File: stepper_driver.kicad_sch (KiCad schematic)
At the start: 8 parts, among them J1 Conn_01x04_Pin, U3 TMC2208_SILENTSTEPSTICK

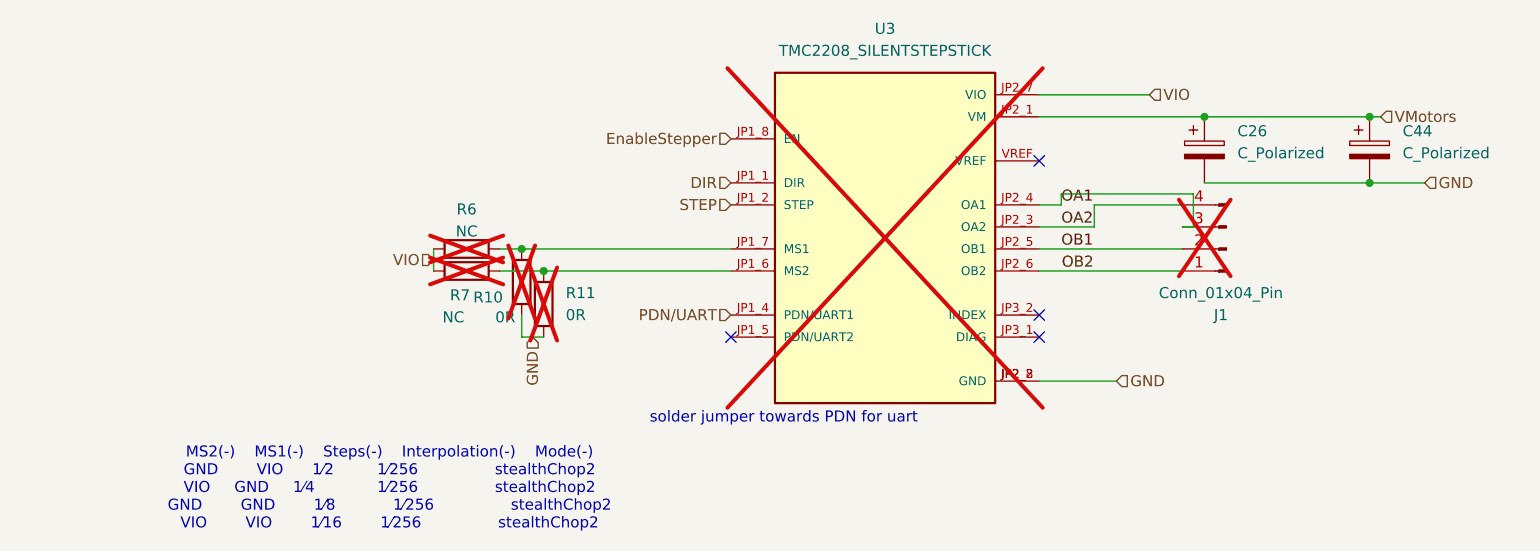
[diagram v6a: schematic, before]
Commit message: fix DNP (was just for checking what was to be bought)
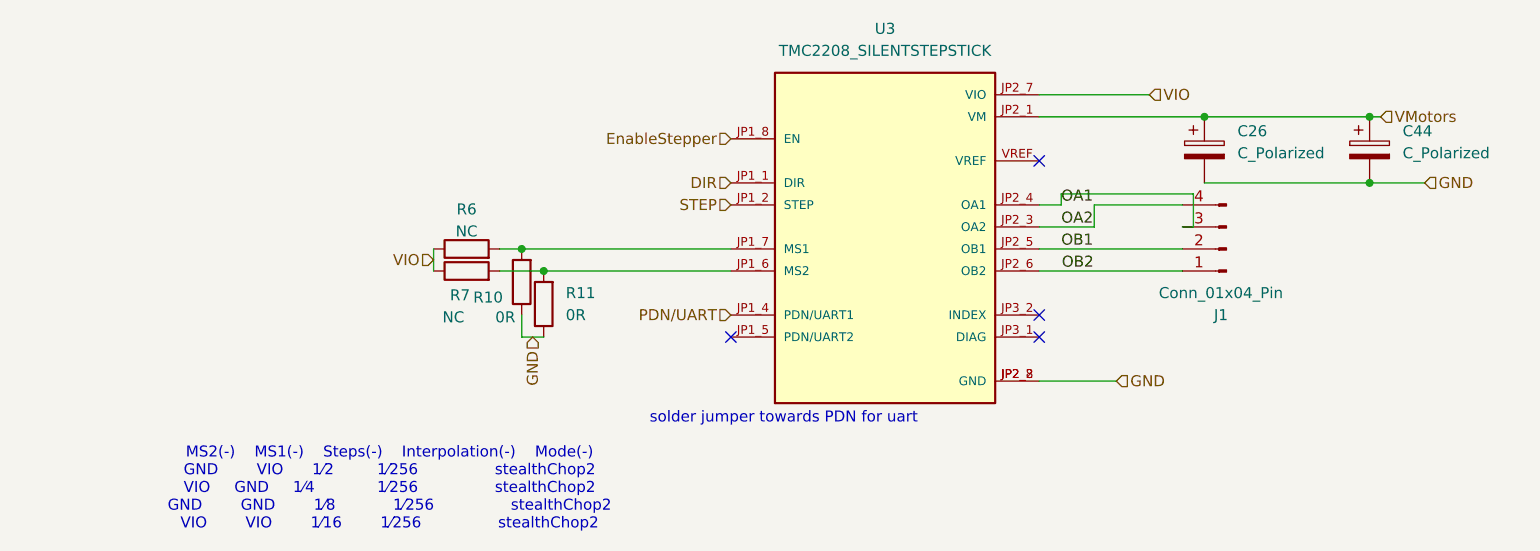
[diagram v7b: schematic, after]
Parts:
- J1, R10, R11, R6, R7, U3: now fitted
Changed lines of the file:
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@@
 		(in_bom yes)
 		(on_board yes)
-		(dnp yes)
+		(dnp no)
 		(property "Reference" "R7"
 			(at 61.468 82.804 90)
@@
 		(in_bom yes)
 		(on_board yes)
-		(dnp yes)
+		(dnp no)
 		(fields_autoplaced yes)
 		(property "Reference" "R11"
@@
 		(in_bom yes)
 		(on_board yes)
-		(dnp yes)
+		(dnp no)
 		(fields_autoplaced yes)
 		(property "Reference" "U3"
@@
 		(in_bom yes)
 		(on_board yes)
-		(dnp yes)
+		(dnp no)
 		(property "Reference" "R10"
 			(at 62.992 83.058 0)
@@
 		(in_bom yes)
 		(on_board yes)
-		(dnp yes)
+		(dnp no)
 		(property "Reference" "R6"
 			(at 62.23 72.898 90)
@@
 		(in_bom yes)
 		(on_board yes)
-		(dnp yes)
+		(dnp no)
 		(property "Reference" "J1"
 			(at 149.225 85.09 0)
